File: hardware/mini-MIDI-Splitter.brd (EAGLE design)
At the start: 138.4 x 19 mm, 40 parts, among them IC1 6N138, IC2 4050D, IC3 REG1117, X1 DIN5PIN, X2 DIN5PIN, X3 DIN5PIN, X4 DIN5PIN, X5 DIN5PIN, X6 DIN5PIN

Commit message: updates
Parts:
- C3: device rcl:E2-4 -> rcl:C0805
- C5: device rcl:C0805 -> rcl:E2-4
- moved C1 59.2 mm to (29.1, 16.3), turned to 270 degrees
- moved C5 44.5 mm to (85.7, 14.1), turned to 0 degrees
- moved R2 25.0 mm to (6.35, 10.2), turned to 90 degrees
- moved C3 17.4 mm to (74.0, 17.0), turned to 180 degrees
- moved C4 15.5 mm to (79.6, 14.1)
- moved C2 14.3 mm to (67.9, 17.0)
- moved R15 14.0 mm to (110.1, 15.2)
- moved R16 14.0 mm to (110.1, 12.7), turned to 0 degrees
- moved R17 14.0 mm to (110.1, 10.2), turned to 180 degrees
- moved R18 14.0 mm to (110.1, 7.62), turned to 0 degrees
- moved R10 13.7 mm to (58.4, 14.0)
- moved R1 11.4 mm to (6.35, 15.2)
- moved R7 11.4 mm to (50.8, 14.0), turned to 270 degrees
- moved R9 11.4 mm to (55.9, 14.0), turned to 270 degrees
- moved IC1 11.4 mm to (12.7, 12.7)
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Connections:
- net GND: now also C3.2, C5.-, R3.1; no longer C3.-, C5.2, R2.1
- net N$1: now also R5.2; no longer R4.2
- net N$11: now also R7.1; no longer R6.1
- net N$12: now also R5.1; no longer R4.1
- net N$14: now also R4.1; no longer R5.1
- net N$15: now also R6.1; no longer R7.1
- net N$16: now also R8.1; no longer R9.1
- net N$18: now also R12.1; no longer R18.1
- net N$19: now also R17.1; no longer R16.1
- net N$2: now also R7.2; no longer R6.2
- net N$20: now also R2.1; no longer R3.1
- net N$21: now also R2.2; no longer R3.2
- net N$22: now also R3.2; no longer R2.2
- net N$3: now also R9.2; no longer R8.2
- net N$5: now also R18.2; no longer R12.2
- net N$6: now also R16.2; no longer R17.2
- net N$7: now also R16.1; no longer R17.1
- net N$8: now also R9.1; no longer R8.1
- net N$9: now also R18.1; no longer R12.1
- net VCC: now also C1.1, C5.+, R12.2, R17.2, R4.2, R6.2, R8.2; no longer C4.+, C5.1, R16.2, R18.2, R5.2, R7.2, R9.2
- net VIN: now also C3.1, C4.+; no longer C1.1, C3.+
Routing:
- net N$18: track 7.42 -> 48.7 mm
- net N$9: track 30.7 -> 71.6 mm
- net N$5: track 48.9 -> 9.49 mm
- net VCC: track 146.5 -> 162.4 mm, vias 1 -> 2
- net N$6: track 13.7 -> 29.5 mm
- net N$11: track 5.02 -> 18.9 mm, vias 0 -> 2
- net N$12: track 17.0 -> 7.85 mm, vias 2 -> 0
- net N$4: track 35.0 -> 43.1 mm
- net N$3: track 20.6 -> 28.6 mm
- net N$26: track 5.82 -> 13.8 mm
- net N$19: track 26.4 -> 19.2 mm
- net N$17: track 42.3 -> 35.2 mm
- net N$23: track 3.06 -> 8.16 mm
- net N$7: track 76.3 -> 80.9 mm
- net N$14: track 11.7 -> 7.55 mm
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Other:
- board size 138.4 x 19 mm -> 140.8 x 19.1 mm
- board text added: "mini midi split rev 2"
- board text removed: "mini midi split rev1"

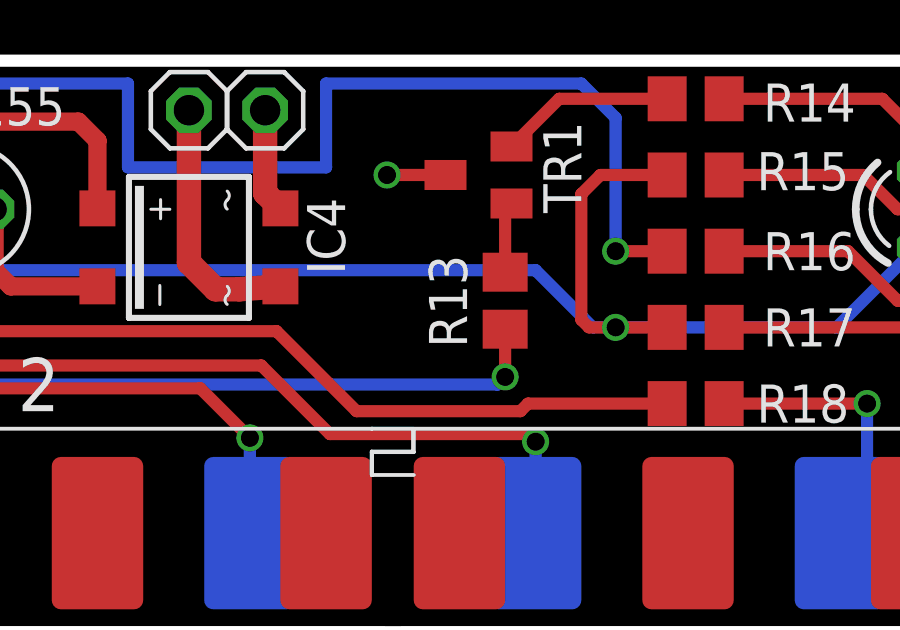
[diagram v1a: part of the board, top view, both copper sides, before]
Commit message: add component values
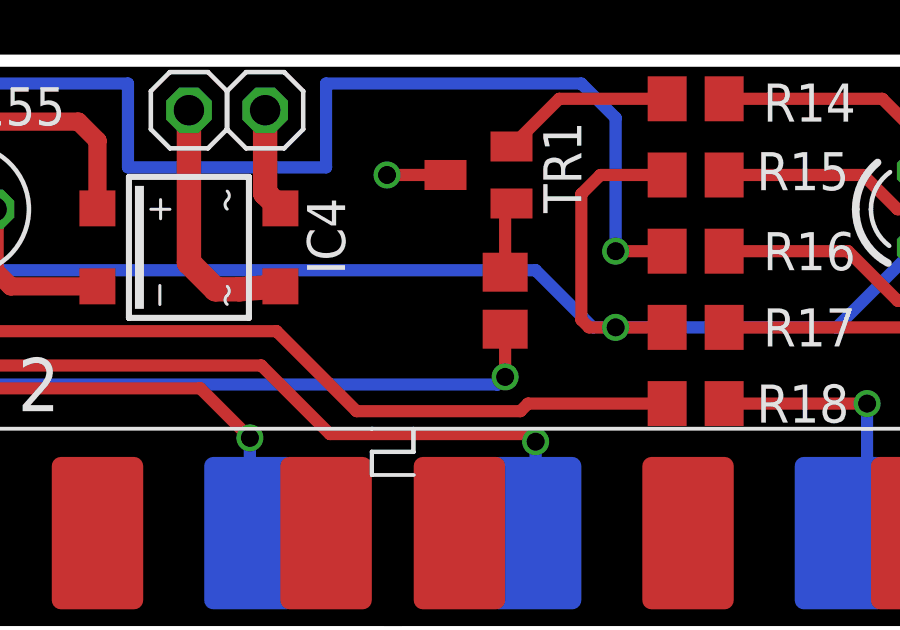
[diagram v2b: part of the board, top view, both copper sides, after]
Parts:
- C2, C3: value (none) -> 100n
- C4, C5: value (none) -> 4u7
- R1, R3: value (none) -> 1k8
- R10, R11, R12, R14, R16, R17, R18, R2, R4, R5, R6, R7, R8, R9: value (none) -> 220r
- R13, R15: value (none) -> 1k
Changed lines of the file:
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@@
 <attribute name="NAME" x="42.799" y="12.954" size="1.27" layer="25" ratio="10"/>
 </element>
-<element name="R5" library="rcl" package="R0805" value="" x="31.75" y="9.906" smashed="yes" rot="R270">
+<element name="R5" library="rcl" package="R0805" value="220r" x="31.75" y="9.906" smashed="yes" rot="R270">
 <attribute name="NAME" x="32.893" y="13.462" size="1.27" layer="25" rot="R180"/>
-<attribute name="VALUE" x="29.21" y="10.541" size="1.27" layer="27" rot="R270"/>
 </element>
-<element name="R7" library="rcl" package="R0805" value="" x="50.8" y="13.97" smashed="yes" rot="R270">
+<element name="R7" library="rcl" package="R0805" value="220r" x="50.8" y="13.97" smashed="yes" rot="R270">
 <attribute name="NAME" x="51.435" y="9.525" size="1.27" layer="25" rot="R90"/>
-<attribute name="VALUE" x="48.26" y="14.605" size="1.27" layer="27" rot="R270"/>
 </element>
-<element name="R11" library="rcl" package="R0805" value="" x="60.96" y="13.97" smashed="yes" rot="R270">
+<element name="R11" library="rcl" package="R0805" value="220r" x="60.96" y="13.97" smashed="yes" rot="R270">
 <attribute name="NAME" x="60.325" y="11.811" size="1.27" layer="25" rot="R270"/>
-<attribute name="VALUE" x="58.42" y="14.605" size="1.27" layer="27" rot="R270"/>
 </element>
-<element name="R18" library="rcl" package="R0805" value="" x="110.109" y="7.62" smashed="yes">
+<element name="R18" library="rcl" package="R0805" value="220r" x="110.109" y="7.62" smashed="yes">
 <attribute name="NAME" x="112.141" y="6.985" size="1.27" layer="25"/>
-<attribute name="VALUE" x="109.474" y="5.08" size="1.27" layer="27"/>
 </element>
-<element name="R9" library="rcl" package="R0805" value="" x="55.88" y="13.97" smashed="yes" rot="R270">
+<element name="R9" library="rcl" package="R0805" value="220r" x="55.88" y="13.97" smashed="yes" rot="R270">
 <attribute name="NAME" x="55.245" y="11.811" size="1.27" layer="25" rot="R270"/>
-<attribute name="VALUE" x="53.34" y="14.605" size="1.27" layer="27" rot="R270"/>
 </element>
-<element name="R16" library="rcl" package="R0805" value="" x="110.109" y="12.7" smashed="yes">
+<element name="R16" library="rcl" package="R0805" value="220r" x="110.109" y="12.7" smashed="yes">
 <attribute name="NAME" x="115.443" y="13.335" size="1.27" layer="25" rot="R180"/>
-<attribute name="VALUE" x="109.474" y="10.16" size="1.27" layer="27"/>
 </element>
-<element name="R4" library="rcl" package="R0805" value="" x="29.083" y="9.906" smashed="yes" rot="R90">
+<element name="R4" library="rcl" package="R0805" value="220r" x="29.083" y="9.906" smashed="yes" rot="R90">
 <attribute name="NAME" x="26.416" y="11.811" size="1.27" layer="25" rot="R270"/>
-<attribute name="VALUE" x="31.623" y="9.271" size="1.27" layer="27" rot="R90"/>
 </element>
-<element name="R6" library="rcl" package="R0805" value="" x="48.26" y="13.97" smashed="yes" rot="R90">
+<element name="R6" library="rcl" package="R0805" value="220r" x="48.26" y="13.97" smashed="yes" rot="R90">
 <attribute name="NAME" x="48.895" y="9.525" size="1.27" layer="25" rot="R90"/>
-<attribute name="VALUE" x="50.8" y="13.335" size="1.27" layer="27" rot="R90"/>
 </element>
-<element name="R8" library="rcl" package="R0805" value="" x="53.34" y="13.97" smashed="yes" rot="R90">
+<element name="R8" library="rcl" package="R0805" value="220r" x="53.34" y="13.97" smashed="yes" rot="R90">
 <attribute name="NAME" x="53.848" y="9.525" size="1.27" layer="25" rot="R90"/>
-<attribute name="VALUE" x="55.88" y="13.335" size="1.27" layer="27" rot="R90"/>
 </element>
-<element name="R10" library="rcl" package="R0805" value="" x="58.42" y="13.97" smashed="yes" rot="R90">
+<element name="R10" library="rcl" package="R0805" value="220r" x="58.42" y="13.97" smashed="yes" rot="R90">
 <attribute name="NAME" x="59.055" y="8.636" size="1.27" layer="25" rot="R90"/>
-<attribute name="VALUE" x="60.96" y="13.335" size="1.27" layer="27" rot="R90"/>
 </element>
-<element name="R12" library="rcl" package="R0805" value="" x="63.5" y="13.97" smashed="yes" rot="R90">
+<element name="R12" library="rcl" package="R0805" value="220r" x="63.5" y="13.97" smashed="yes" rot="R90">
 <attribute name="NAME" x="64.135" y="8.636" size="1.27" layer="25" rot="R90"/>
-<attribute name="VALUE" x="66.04" y="13.335" size="1.27" layer="27" rot="R90"/>
 </element>
-<element name="R17" library="rcl" package="R0805" value="" x="110.109" y="10.16" smashed="yes" rot="R180">
+<element name="R17" library="rcl" package="R0805" value="220r" x="110.109" y="10.16" smashed="yes" rot="R180">
 <attribute name="NAME" x="115.443" y="10.795" size="1.27" layer="25" rot="R180"/>
-<attribute name="VALUE" x="110.744" y="12.7" size="1.27" layer="27" rot="R180"/>
 </element>
 <element name="IC1" library="optocoupler" package="DIL08" value="6N138" x="12.7" y="12.7" smashed="yes">
@@
 <attribute name="NAME" x="4.699" y="13.081" size="1.27" layer="25" ratio="10" rot="R180"/>
 </element>
-<element name="R2" library="rcl" package="R0805" value="" x="6.35" y="10.16" smashed="yes" rot="R90">
+<element name="R2" library="rcl" package="R0805" value="220r" x="6.35" y="10.16" smashed="yes" rot="R90">
 <attribute name="NAME" x="3.556" y="10.922" size="1.27" layer="25" rot="R270"/>
-<attribute name="VALUE" x="8.89" y="9.525" size="1.27" layer="27" rot="R90"/>
 </element>
-<element name="R1" library="rcl" package="R0805" value="" x="6.35" y="15.24" smashed="yes" rot="R270">
+<element name="R1" library="rcl" package="R0805" value="1k8" x="6.35" y="15.24" smashed="yes" rot="R270">
 <attribute name="NAME" x="3.556" y="16.637" size="1.27" layer="25" rot="R270"/>
-<attribute name="VALUE" x="3.81" y="15.875" size="1.27" layer="27" rot="R270"/>
 </element>
-<element name="R3" library="rcl" package="R0805" value="" x="19.05" y="15.24" smashed="yes" rot="R270">
+<element name="R3" library="rcl" package="R0805" value="1k8" x="19.05" y="15.24" smashed="yes" rot="R270">
 <attribute name="NAME" x="20.574" y="16.637" size="1.27" layer="25" rot="R270"/>
-<attribute name="VALUE" x="16.51" y="15.875" size="1.27" layer="27" rot="R270"/>
 </element>
 <element name="IC3" library="burr-brown" package="SOT223" value="REG1117" x="71.12" y="12.7" smashed="yes" rot="R90">
@@
 <attribute name="VALUE" x="106.045" y="13.335" size="1.27" layer="27" rot="R90"/>
 </element>
-<element name="R14" library="rcl" package="R0805" value="" x="110.109" y="17.78" smashed="yes">
+<element name="R14" library="rcl" package="R0805" value="220r" x="110.109" y="17.78" smashed="yes">
 <attribute name="NAME" x="115.443" y="18.288" size="1.27" layer="25" rot="R180"/>
-<attribute name="VALUE" x="109.474" y="15.24" size="1.27" layer="27"/>
 </element>
-<element name="R13" library="rcl" package="R0805" value="" x="103.759" y="11.049" smashed="yes" rot="R270">
-<attribute name="NAME" x="101.219" y="12.573" size="1.27" layer="25" rot="R270"/>
-<attribute name="VALUE" x="101.219" y="11.684" size="1.27" layer="27" rot="R270"/>
-</element>
+<element name="R13" library="rcl" package="R0805" value="1k" x="103.759" y="11.049" smashed="yes" rot="R270"/>
 <element name="LED1" library="led" package="LED3MM" value="" x="117.475" y="14.097" smashed="yes" rot="R90">
 <attribute name="NAME" x="121.539" y="17.526" size="1.27" layer="25" ratio="10" rot="R180"/>
@@
 <attribute name="VALUE" x="125.476" y="16.002" size="1.27" layer="27" ratio="10" rot="R90"/>
 </element>
-<element name="R15" library="rcl" package="R0805" value="" x="110.109" y="15.24" smashed="yes" rot="R180">
+<element name="R15" library="rcl" package="R0805" value="1k" x="110.109" y="15.24" smashed="yes" rot="R180">
 <attribute name="NAME" x="112.141" y="14.732" size="1.27" layer="25"/>
-<attribute name="VALUE" x="110.744" y="17.78" size="1.27" layer="27" rot="R180"/>
 </element>
-<element name="C3" library="rcl" package="C0805" value="" x="74.041" y="17.018" smashed="yes" rot="R180">
+<element name="C3" library="rcl" package="C0805" value="100n" x="74.041" y="17.018" smashed="yes" rot="R180">
 <attribute name="NAME" x="76.327" y="18.161" size="1.27" layer="25" rot="R270"/>
-<attribute name="VALUE" x="75.311" y="19.558" size="1.27" layer="27" rot="R180"/>
 </element>
-<element name="C2" library="rcl" package="C0805" value="" x="67.945" y="17.018" smashed="yes">
+<element name="C2" library="rcl" package="C0805" value="100n" x="67.945" y="17.018" smashed="yes">
 <attribute name="NAME" x="64.389" y="18.161" size="1.27" layer="25" rot="R270"/>
-<attribute name="VALUE" x="66.675" y="14.478" size="1.27" layer="27"/>
 </element>
-<element name="C4" library="rcl" package="E2-4" value="" x="79.629" y="14.097" smashed="yes">
+<element name="C4" library="rcl" package="E2-4" value="4u7" x="79.629" y="14.097" smashed="yes">
 <attribute name="NAME" x="78.486" y="10.16" size="1.27" layer="25" ratio="10"/>
-<attribute name="VALUE" x="81.788" y="11.938" size="1.27" layer="27" ratio="10"/>
 </element>
-<element name="C5" library="rcl" package="E2-4" value="" x="85.725" y="14.097" smashed="yes">
+<element name="C5" library="rcl" package="E2-4" value="4u7" x="85.725" y="14.097" smashed="yes">
 <attribute name="NAME" x="84.709" y="10.033" size="1.27" layer="25" ratio="10"/>
-<attribute name="VALUE" x="87.884" y="11.938" size="1.27" layer="27" ratio="10"/>
 </element>
 <element name="D1" library="jasons_stuff" package="0805DIODE" value="0805DIODE" x="19.05" y="10.16" smashed="yes" rot="R270">

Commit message: REV3 PCB
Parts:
- removed GND, VIN: (no value), pinhead:1X01
- removed TR1: (no value), transistor:SOT23-BEC
- added C6: 4u7, rcl:E2-4
- added DAT: (no value), led:LED3MM
- added IC5: (no value), microbuilder:SOIC-4
- added ICSP: (no value), tag-connect:TC2030-MCP-NL
- added RA2, RA4: (no value), pinhead:1X01
- added U$1: PWR_SOCKET_2_1MM, jason_eagle6:PWR_SOCKET_2_1MM
- added X7: VERTICAL_3_5MM_SOCKET, jason_eagle6:VERTICAL_3_5MM_SOCKET
- C1: value (none) -> 100n
- C3: value 100n -> (none)
- C4: value 4u7 -> 100n; device rcl:E2-4 -> rcl:C0805
- IC1: value 6N138 -> REG1117; device optocoupler:DIL08 -> burr-brown:SOT223
- IC3: value REG1117 -> PIC12F1822SO08; device burr-brown:SOT223 -> jasons_stuff:SO08
- IC4: value (none) -> 6N138; device microbuilder:SOIC-4 -> optocoupler:DIL08
- R1: value 1k8 -> 1k
- R13, R15: value 1k -> 220r
- R17, R18: value 220r -> 1k8
- R3: value 1k8 -> 220r
- moved R1 117.6 mm to (123.8, 10.8), flipped to the bottom, turned to 180 degrees
- moved R2 111.1 mm to (117.5, 10.8), flipped to the bottom, turned to 180 degrees
- moved R4 102.5 mm to (131.4, 3.94), flipped to the bottom, turned to 270 degrees
- moved R16 100.8 mm to (9.65, 3.81), flipped to the bottom, turned to 90 degrees
- moved R5 96.1 mm to (127.6, 3.94), flipped to the bottom, turned to 90 degrees
- moved R3 92.4 mm to (111.4, 10.7), flipped to the bottom, turned to 180 degrees
- moved R17 84.8 mm to (25.4, 15.0), flipped to the bottom, turned to 90 degrees
- moved R18 84.8 mm to (25.4, 10.4), flipped to the bottom, turned to 90 degrees
- moved R15 81.6 mm to (29.3, 3.94), flipped to the bottom, turned to 90 degrees
- moved R14 78.6 mm to (32.8, 3.94), flipped to the bottom, turned to 270 degrees
- moved IC1 76.2 mm to (88.9, 15.0), flipped to the bottom, turned to 180 degrees
- moved IC4 69.1 mm to (24.1, 12.7), turned to 270 degrees
- moved C1 64.7 mm to (93.7, 15.1), flipped to the bottom
- moved R6 64.2 mm to (111.6, 3.94), flipped to the bottom, turned to 270 degrees
- moved R7 58.1 mm to (108.1, 3.94), flipped to the bottom, turned to 90 degrees
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- renumbered LED1 to CLK, LED2 to PWR
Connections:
- removed net DAT: IC1.6, IC2.11, IC2.14, IC2.3, IC2.5, IC2.7, IC2.9, R1.2, R13.2
- removed net N$26: PWR.A, R15.1
- new net CLK: CLK.K, R2.2
- new net CLK_LED: CLK.A, IC3.6, ICSP.5
- new net DAT_LED: DAT.A, IC3.7, ICSP.4
- new net MIDI_IN: IC2.11, IC2.14, IC2.3, IC2.5, IC2.7, IC2.9, IC3.2, IC4.6, R18.2
- new net MIDI_OUT: IC3.3, RA4.1
- new net N$33: IC3.4, ICSP.1
- net GND: now also C4.2, C6.-, IC1.1, IC3.8, IC4.5, IC5.-, ICSP.3, R1.1, R17.1, R2.1; no longer C4.-, IC1.5, IC3.1, IC4.-, PWR.K, TR1.C
- net N$1: now also R14.2; no longer R5.2
- net N$10: now also R8.1; no longer R11.1
- net N$11: now also IC2.2, R4.1; no longer IC2.4, R7.1
- net N$12: now also IC2.4, R6.1; no longer IC2.2, R5.1
- net N$13: now also PWR.K, R1.2; no longer R14.1, TR1.E
- net N$14: now also R15.1; no longer R4.1
- net N$15: now also R13.1; no longer R6.1
- net N$16: now also R11.1; no longer R8.1
- net N$17: now also R9.1; no longer R10.1
- net N$18: now also R7.1; no longer R12.1
- net N$19: now also R5.1; no longer R17.1
- net N$2: now also R12.2; no longer R7.2
- net N$20: now also R16.1, X7.4; no longer R2.1
- net N$21: now also IC4.2, R16.2; no longer IC1.2, R2.2
- net N$22: now also IC4.7, R17.2; no longer IC1.7, R3.2
- net N$23: now also DAT.K, R3.2; no longer CLK.K, R14.2
- net N$24: now also IC4.3, X7.3; no longer IC1.3
- net N$25: now also IC3.5, RA2.1; no longer R13.1, TR1.B
- net N$27: now also IC5.~1, U$1.BARREL; no longer IC4.~1, VIN.1
- net N$28: now also IC5.~2, U$1.PIN; no longer GND.1, IC4.~2
- net N$3: now also R10.2; no longer R9.2
- net N$4: now also R8.2; no longer R11.2
- net N$5: now also R6.2; no longer R18.2
- net N$6: now also R4.2; no longer R16.2
- net N$7: now also R14.1; no longer R16.1
- net N$8: now also R12.1; no longer R9.1
- net N$9: now also R10.1; no longer R18.1
- net VCC: now also C3.1, C4.1, IC1.2, IC3.1, IC4.8, ICSP.2, PWR.A, R11.2, R13.2, R18.1, R5.2, R7.2, R9.2; no longer C1.1, CLK.A, IC1.8, IC3.2, R1.1, R10.2, R12.2, R17.2, R4.2, R6.2, R8.2
- net VIN: now also C1.1, C6.+, IC1.3, IC5.+; no longer C3.1, C4.+, IC3.3, IC4.+
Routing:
- net DAT: track 127.5 -> 0.00 mm, vias 3 -> 0
- net VCC: track 162.4 -> 269.7 mm, vias 2 -> 8
- net DAT_LED: track 0.00 -> 92.9 mm, vias 0 -> 2
- net CLK_LED: track 0.00 -> 88.0 mm, vias 0 -> 1
- net MIDI_IN: track 0.00 -> 81.3 mm, vias 0 -> 2
- net N$9: track 71.6 -> 7.77 mm, vias 2 -> 0
- net N$11: track 18.9 -> 65.0 mm, vias 2 -> 0
- net N$18: track 48.7 -> 3.43 mm, vias 1 -> 0
- net N$7: track 80.9 -> 41.3 mm, vias 2 -> 0
- net N$4: track 43.1 -> 3.56 mm, vias 1 -> 0
- net N$12: track 7.85 -> 43.0 mm
- net N$17: track 35.2 -> 3.56 mm, vias 1 -> 0
- net N$6: track 29.5 -> 3.31 mm, vias 1 -> 0
- net N$3: track 28.6 -> 3.56 mm, vias 1 -> 0
- net N$28: track 3.48 -> 28.4 mm
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- added copper zone on layer 1, net GND
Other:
- board size 140.8 x 19.1 mm -> 140.8 x 20.7 mm
- board text added: "banana split"
- board text added: "rev 3"
- board text added: "six4pix.com/split"
- board text removed: "mini midi split rev 2"

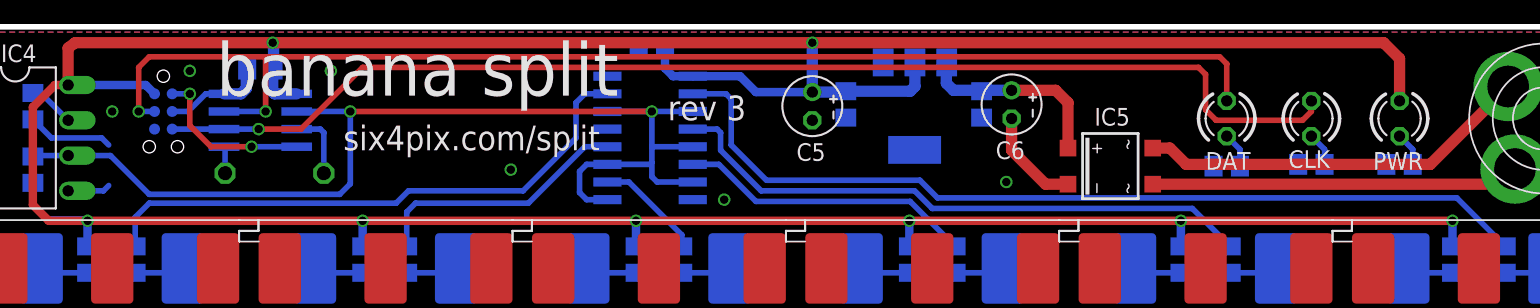
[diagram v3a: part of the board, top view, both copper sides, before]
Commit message: V4 - Grounding output GND pins!
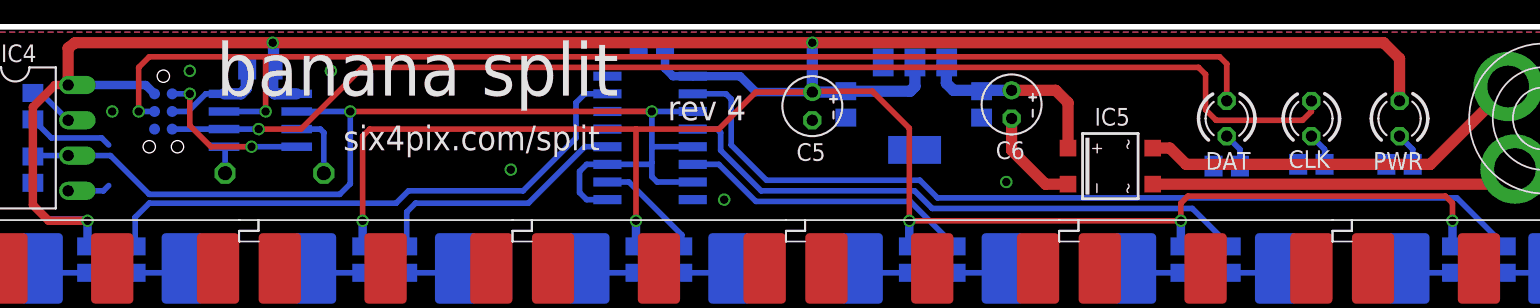
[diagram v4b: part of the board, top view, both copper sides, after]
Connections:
- net GND: now also X1.2, X2.2, X3.2, X4.2, X5.2, X6.2
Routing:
- net VCC: track 269.7 -> 274.6 mm
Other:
- board text added: "rev 4"
- board text removed: "rev 3"
